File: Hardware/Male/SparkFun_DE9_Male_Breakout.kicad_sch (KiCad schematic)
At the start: 9 parts, among them J1 Conn_01x01, J2 Conn_01x09, J3 DE9 Header, J4 Conn_01x01

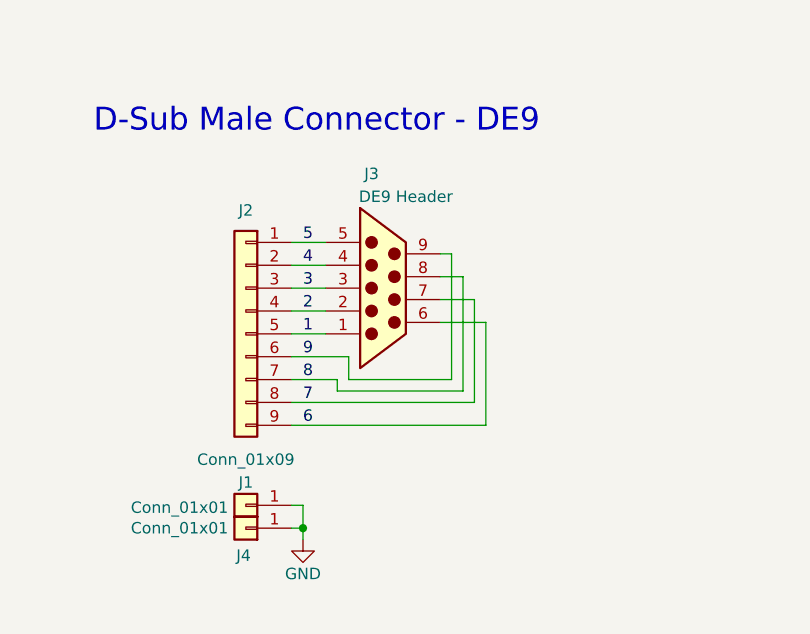
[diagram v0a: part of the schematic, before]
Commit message: Fix pin layout
Adds model for female socket
FIxes male footprint and symbol; updates schematic and PCB
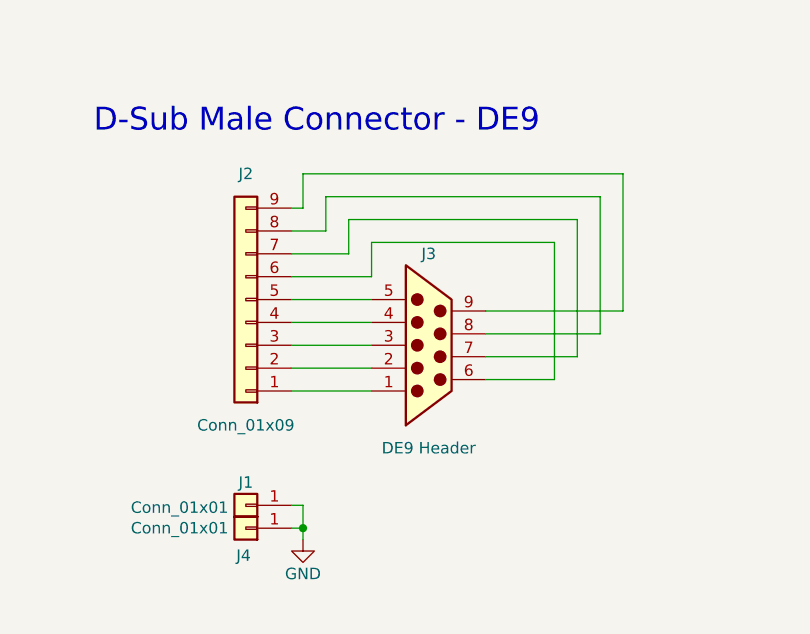
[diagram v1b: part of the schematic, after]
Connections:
- net 1: no longer names the net of J3.1
- net 1: now also J2.1 (Pin_1); no longer J2.5 (Pin_5)
- net 2: no longer names the net of J3.2
- net 2: now also J2.2 (Pin_2); no longer J2.4 (Pin_4)
- net 3: no longer names the net of J2.3 (Pin_3), J3.3
- net 4: no longer names the net of J3.4
- net 4: now also J2.4 (Pin_4); no longer J2.2 (Pin_2)
- net 5: no longer names the net of J3.5
- net 5: now also J2.5 (Pin_5); no longer J2.1 (Pin_1)
- net 6: no longer names the net of J3.6
- net 6: now also J2.6 (Pin_6); no longer J2.9 (Pin_9)
- net 7: no longer names the net of J3.7
- net 7: now also J2.7 (Pin_7); no longer J2.8 (Pin_8)
- net 8: no longer names the net of J3.8
- net 8: now also J2.8 (Pin_8); no longer J2.7 (Pin_7)
- net 9: no longer names the net of J3.9
- net 9: now also J2.9 (Pin_9); no longer J2.6 (Pin_6)
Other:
- moved on the sheet: J2
